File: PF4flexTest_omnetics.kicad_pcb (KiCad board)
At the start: 4 copper layers, 82.5 x 93.5 mm, 8 parts, among them J1 Conn_02x25_Top_Bottom

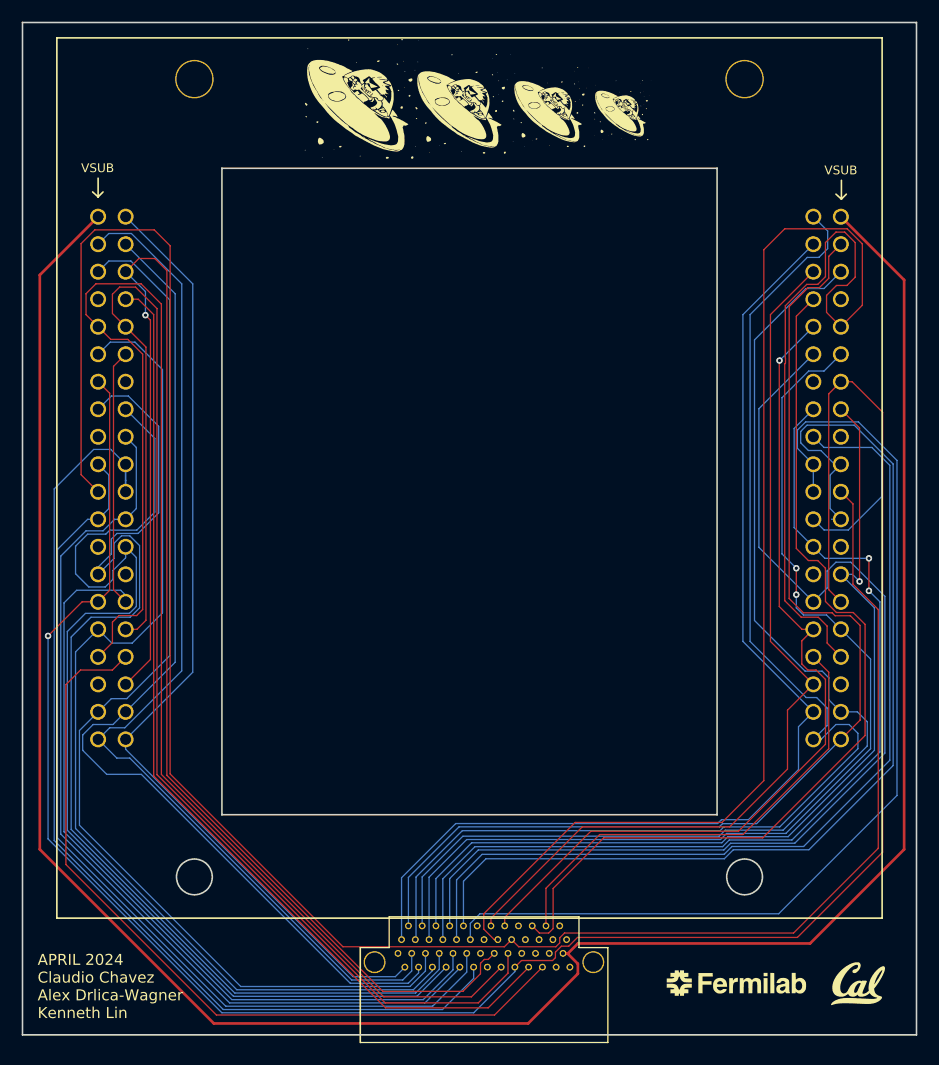
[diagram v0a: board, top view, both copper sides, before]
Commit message: Minor improvements with routing
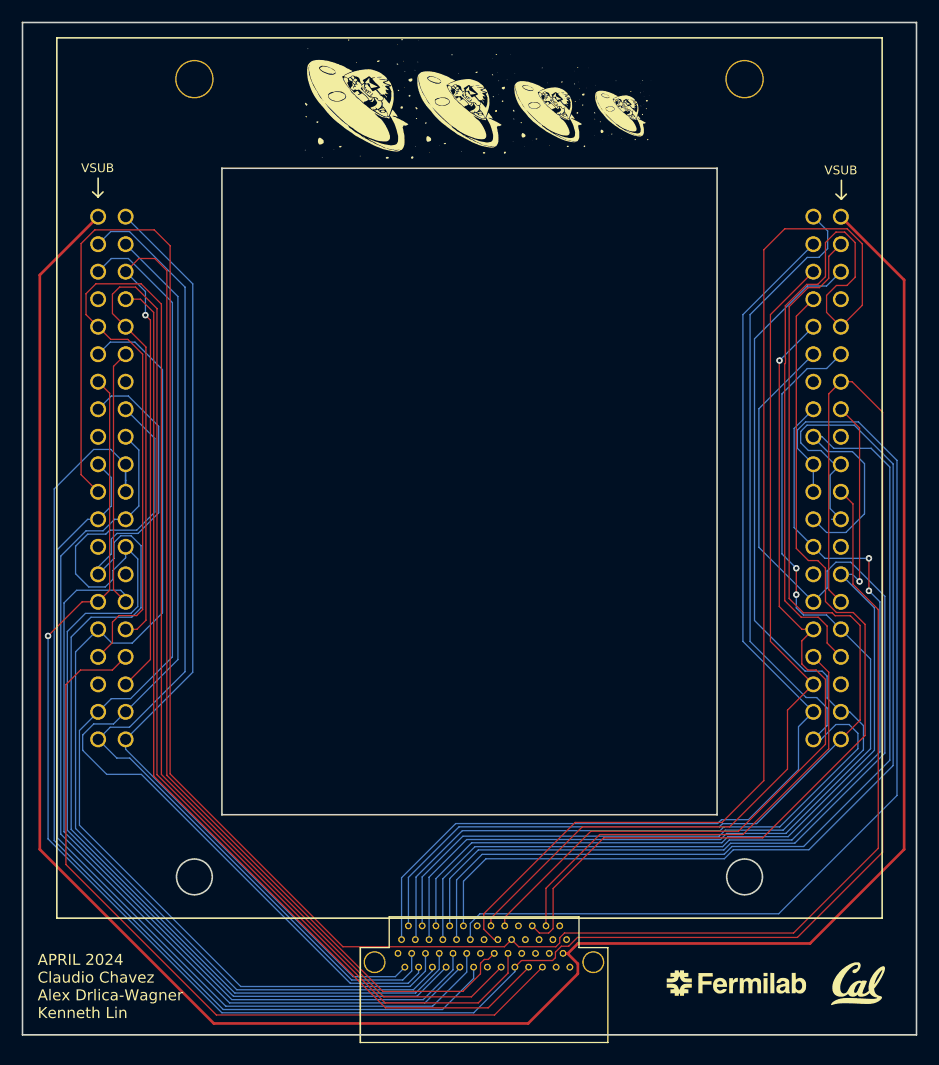
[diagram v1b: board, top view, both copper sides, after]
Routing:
- net V1_U: track 97.1 -> 101.7 mm
- net RG_U: track 105.4 -> 104.8 mm
- net H2: track 200.1 -> 200.7 mm
- net RG_L: track 101.6 -> 102.2 mm
